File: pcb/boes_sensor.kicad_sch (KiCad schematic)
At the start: 11 parts, among them U1 LM358

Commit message: Add finished sensor PCB
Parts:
- added TP2: Output, Connector_Wire:SolderWire-0.25sqmm_1x01_D0.65mm_OD1.7mm_Relief, symbol Connector:TestPoint
- added TP3: VCC, Connector_Wire:SolderWire-0.25sqmm_1x01_D0.65mm_OD1.7mm_Relief, symbol Connector:TestPoint
- added TP4: GND, Connector_Wire:SolderWire-0.25sqmm_1x01_D0.65mm_OD1.7mm_Relief, symbol Connector:TestPoint
- added unit 2 of U1
- C1: footprint (none) -> Capacitor_SMD:C_0603_1608Metric
- C2: renamed from C?; footprint (none) -> Capacitor_SMD:C_0603_1608Metric
- D2: footprint (none) -> Diode_SMD:D_MiniMELF
- R1, R3: footprint (none) -> Resistor_SMD:R_0603_1608Metric
- R2, R4: renamed from R?; footprint (none) -> Resistor_SMD:R_0603_1608Metric
- U1: renamed from U?; footprint (none) -> Package_SO:SOIC-8_3.9x4.9mm_P1.27mm
- U1: footprint (none) -> Package_SO:SOIC-8_3.9x4.9mm_P1.27mm
- Y1: renamed from Y?; footprint (none) -> Connector_Wire:SolderWire-0.1sqmm_1x02_P3.6mm_D0.4mm_OD1mm_Relief
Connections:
- net GND: now also C1.2, D1.3 (K), R2.2, R3.2, Y1.1, TP4.1
- net Output: now also TP2.1, U1.6 (-), U1.7; no longer C1.1, D2.1 (K), R3.1, R4.1
- net +5V renamed VCC
- net VCC: now also TP3.1
- new net: C1.1, D2.1 (K), R3.1, R4.1, U1.5 (+)
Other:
- moved on the sheet: C2, D1, R4

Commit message: Use teardrop pads for sensor PCB
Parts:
- renumbered C2 to C1, C1 to C2, R4 to R3, R3 to R4, TP3 to TP1, TP4 to TP2, TP2 to TP3

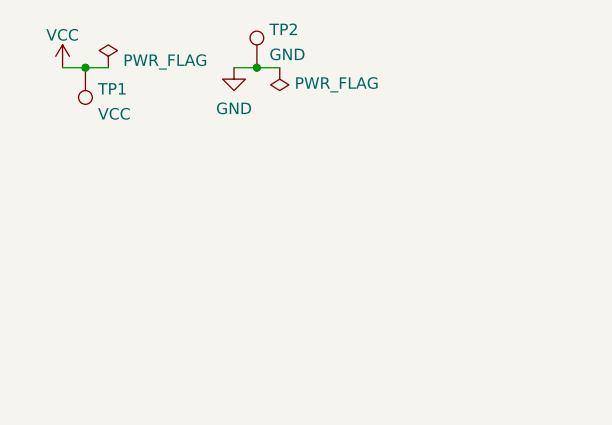
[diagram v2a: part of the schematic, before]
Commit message: Add decoupling to sensor VCC rail
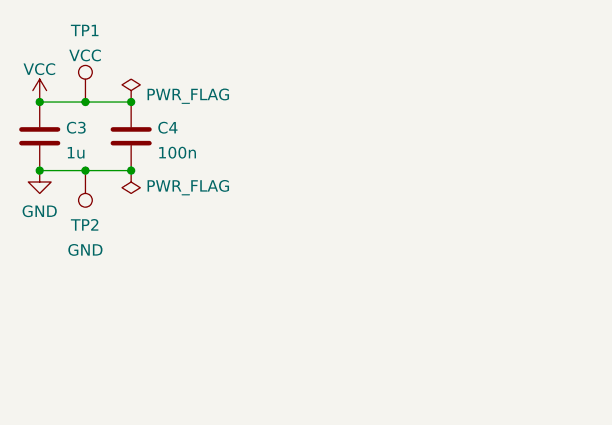
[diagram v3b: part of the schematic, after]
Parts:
- added C3: 1u, Capacitor_SMD:C_0603_1608Metric, symbol Device:C
- added C4: 100n, Capacitor_SMD:C_0603_1608Metric, symbol Device:C
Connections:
- net GND: now also C3.2, C4.2
- net VCC: now also C3.1, C4.1
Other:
- moved on the sheet: TP1, TP2
